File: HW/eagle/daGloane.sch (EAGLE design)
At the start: 83 parts, among them IC1 MCP1252-33X50, U1 STM32F10XTXU6, X2 USB_MICROB_PLUG_MT

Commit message: changed some values
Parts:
- C4: value 4.7 -> 4.7u
- R14, R19: value 150R -> 270R
- R29: value 330 -> 470R
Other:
- note added: "Value changed"
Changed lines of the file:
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@@
 <?xml version="1.0" encoding="utf-8"?>
 <!DOCTYPE eagle SYSTEM "eagle.dtd">
-<eagle version="6.1">
+<eagle version="6.2">
 <drawing>
 <settings>
@@
 <part name="U$3" library="daGloane" deviceset="MPU6000" device=""/>
 <part name="U$4" library="daGloane" deviceset="SERIAL_FT230XQ" device=""/>
-<part name="R14" library="rcl" deviceset="R-EU_" device="R0603" value="150R"/>
-<part name="R19" library="rcl" deviceset="R-EU_" device="R0603" value="150R"/>
+<part name="R14" library="rcl" deviceset="R-EU_" device="R0603" value="270R"/>
+<part name="R19" library="rcl" deviceset="R-EU_" device="R0603" value="270R"/>
 <part name="R11" library="rcl" deviceset="R-EU_" device="R0603" value="27R"/>
 <part name="R13" library="rcl" deviceset="R-EU_" device="R0603" value="27R"/>
@@
 <part name="GND28" library="supply1" deviceset="GND" device=""/>
 <part name="GND29" library="supply1" deviceset="GND" device=""/>
-<part name="C4" library="rcl" deviceset="C-EU" device="C0603" value="4.7"/>
+<part name="C4" library="rcl" deviceset="C-EU" device="C0603" value="4.7u"/>
 <part name="GND30" library="supply1" deviceset="GND" device=""/>
 <part name="LIPO+" library="testpad" deviceset="TPS" device="PAD1-13"/>
@@
 <part name="3.3V5" library="supply1" deviceset="VCC" device="" value="3.3V"/>
 <part name="LED5" library="led" deviceset="LED" device="CHIPLED_0603"/>
-<part name="R29" library="rcl" deviceset="R-EU_" device="R0603" value="330"/>
+<part name="R29" library="rcl" deviceset="R-EU_" device="R0603" value="470R"/>
 <part name="C30" library="rcl" deviceset="C-EU" device="C0805" value="10µF/6.3V"/>
 <part name="C31" library="rcl" deviceset="C-EU" device="C0805" value="10µF/6.3V"/>
@@
 <text x="193.04" y="-320.04" size="1.778" layer="91">for bluetooth communction it has to be reset </text>
 <text x="193.04" y="-322.58" size="1.778" layer="91">by the µC using the "AT+RESET" command</text>
+<text x="60.96" y="-175.26" size="1.778" layer="91" rot="R270">Value changed</text>
+<text x="132.08" y="-373.38" size="1.778" layer="91" rot="R270">Value changed</text>
 </plain>
 <instances>

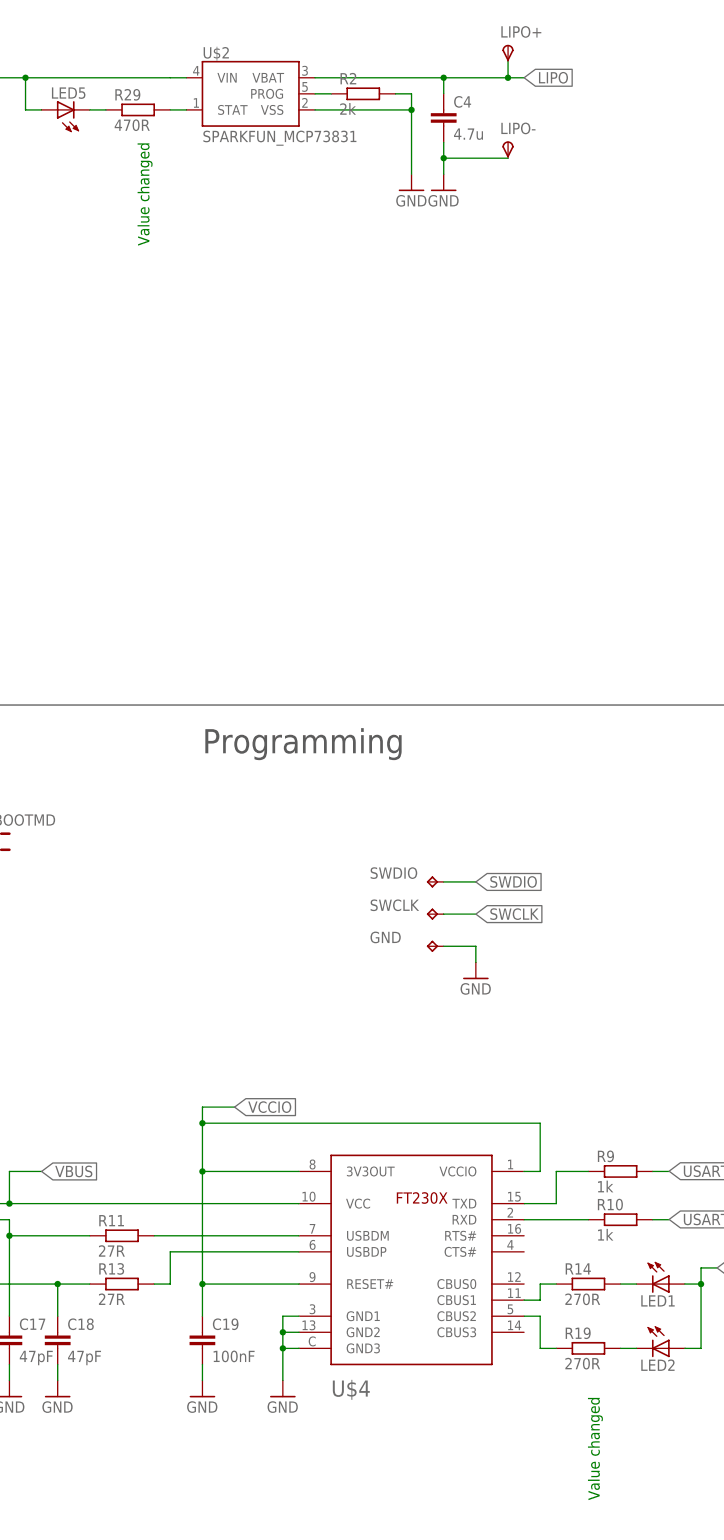
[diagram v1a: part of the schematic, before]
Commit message: resistor values for LEDs changed back; voltage drop over LEDs at 10mA is 2V. Therefore the voltage drop accross the resistor has to be 1.3V (3.3V supply) --> R = 1.3V / 10mA = 130Ohm; next E12 value is 150Ohm.
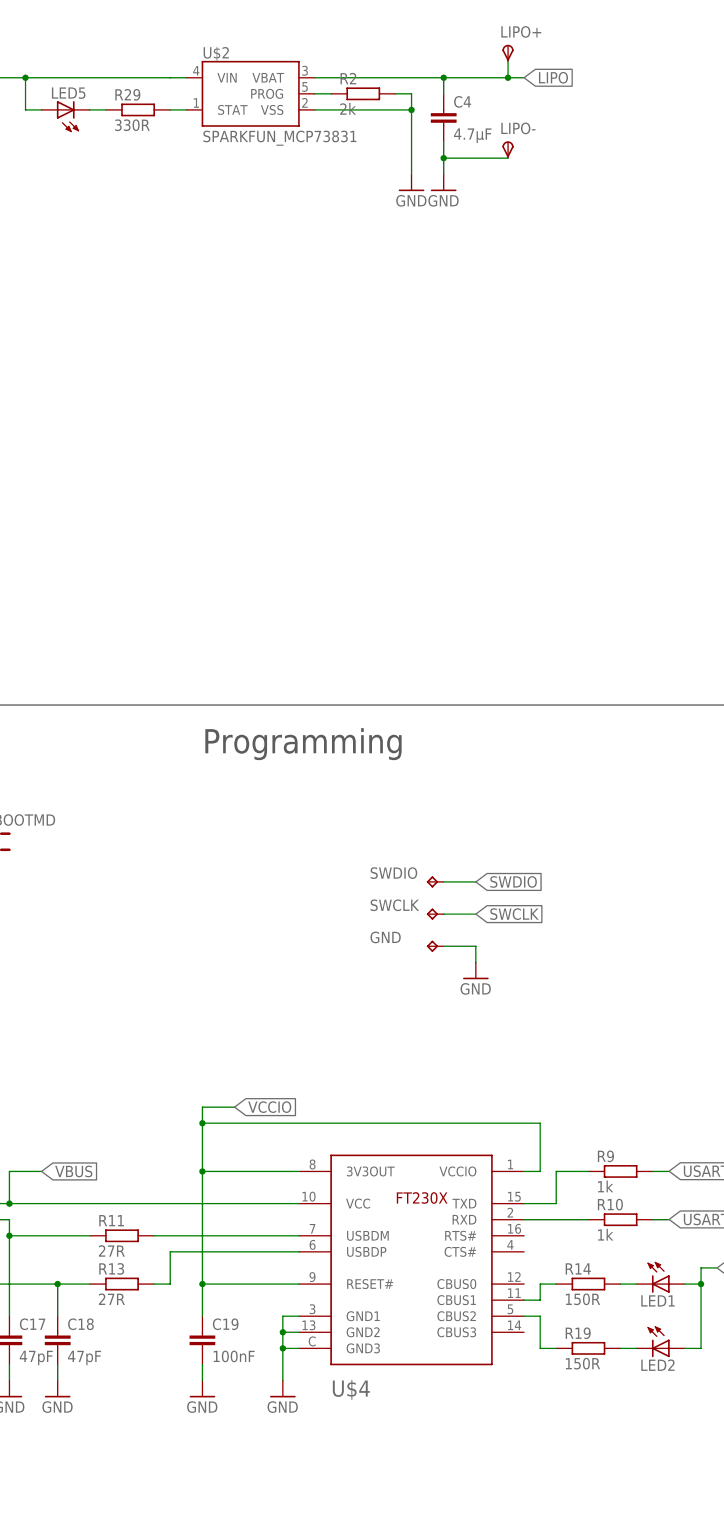
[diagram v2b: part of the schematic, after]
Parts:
- C4: value 4.7u -> 4.7µF
- R14, R19: value 270R -> 150R
- R29: value 470R -> 330R
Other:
- note removed: "Value changed"
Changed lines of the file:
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@@
 <part name="U$3" library="daGloane" deviceset="MPU6000" device=""/>
 <part name="U$4" library="daGloane" deviceset="SERIAL_FT230XQ" device=""/>
-<part name="R14" library="rcl" deviceset="R-EU_" device="R0603" value="270R"/>
-<part name="R19" library="rcl" deviceset="R-EU_" device="R0603" value="270R"/>
+<part name="R14" library="rcl" deviceset="R-EU_" device="R0603" value="150R"/>
+<part name="R19" library="rcl" deviceset="R-EU_" device="R0603" value="150R"/>
 <part name="R11" library="rcl" deviceset="R-EU_" device="R0603" value="27R"/>
 <part name="R13" library="rcl" deviceset="R-EU_" device="R0603" value="27R"/>
@@
 <part name="GND28" library="supply1" deviceset="GND" device=""/>
 <part name="GND29" library="supply1" deviceset="GND" device=""/>
-<part name="C4" library="rcl" deviceset="C-EU" device="C0603" value="4.7u"/>
+<part name="C4" library="rcl" deviceset="C-EU" device="C0603" value="4.7µF"/>
 <part name="GND30" library="supply1" deviceset="GND" device=""/>
 <part name="LIPO+" library="testpad" deviceset="TPS" device="PAD1-13"/>
@@
 <part name="3.3V5" library="supply1" deviceset="VCC" device="" value="3.3V"/>
 <part name="LED5" library="led" deviceset="LED" device="CHIPLED_0603"/>
-<part name="R29" library="rcl" deviceset="R-EU_" device="R0603" value="470R"/>
+<part name="R29" library="rcl" deviceset="R-EU_" device="R0603" value="330R"/>
 <part name="C30" library="rcl" deviceset="C-EU" device="C0805" value="10µF/6.3V"/>
 <part name="C31" library="rcl" deviceset="C-EU" device="C0805" value="10µF/6.3V"/>
@@
 <text x="193.04" y="-320.04" size="1.778" layer="91">for bluetooth communction it has to be reset </text>
 <text x="193.04" y="-322.58" size="1.778" layer="91">by the µC using the "AT+RESET" command</text>
-<text x="60.96" y="-175.26" size="1.778" layer="91" rot="R270">Value changed</text>
-<text x="132.08" y="-373.38" size="1.778" layer="91" rot="R270">Value changed</text>
 </plain>
 <instances>
